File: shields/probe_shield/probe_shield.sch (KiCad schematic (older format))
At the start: 11 parts

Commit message: finished probe shield schematics
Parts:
- added J5: GPIO shield connector 40pin, symbol Connector_Generic:Conn_02x20_Odd_Even
- added J6: probe shield connector 20pin, symbol Connector_Generic:Conn_02x10_Odd_Even
- gave numbers to parts that had none: 11
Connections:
- net +5V: now also J5.2 (Pin_2), J5.4 (Pin_4)
- net GND: now also J5.14 (Pin_14), J5.20 (Pin_20), J5.25 (Pin_25), J5.30 (Pin_30), J5.34 (Pin_34), J5.39 (Pin_39), J5.6 (Pin_6), J5.9 (Pin_9)
- net RST_0: now also J6.9 (Pin_9); no longer J4.10 (~RESET~)
- net RST_1: now also J6.10 (Pin_10)
- net RST_2: now also J6.19 (Pin_19)
- net TCK|SWDCLK_0: now also J6.3 (Pin_3); no longer J4.04 (SWDCLK/TCK)
- net TCK|SWDCLK_1: now also J6.4 (Pin_4)
- net TCK|SWDCLK_2: now also J6.13 (Pin_13)
- net TDI|NC_0: now also J6.7 (Pin_7); no longer J4.08 (NC/TDI)
- net TDI|NC_1: now also J6.8 (Pin_8)
- net TDI|NC_2: now also J6.17 (Pin_17)
- net TDO|SWO_0: now also J6.5 (Pin_5); no longer J4.06 (SWO/TDO)
- net TDO|SWO_1: now also J6.6 (Pin_6)
- net TDO|SWO_2: now also J6.15 (Pin_15)
- net TMS|SWDIO_0: now also J6.1 (Pin_1); no longer J4.02 (SWDIO/TMS)
- net TMS|SWDIO_1: now also J6.2 (Pin_2)
- net TMS|SWDIO_2: now also J6.11 (Pin_11)
- new net RST_3: J4.10 (~RESET~), J6.20 (Pin_20)
- new net TCK|SWDCLK_3: J4.04 (SWDCLK/TCK), J6.14 (Pin_14)
- new net TDI|NC_3: J4.08 (NC/TDI), J6.18 (Pin_18)
- new net TDO|SWO_3: J4.06 (SWO/TDO), J6.16 (Pin_16)
- new net TMS|SWDIO_3: J4.02 (SWDIO/TMS), J6.12 (Pin_12)
- no-connect marks 1 -> 31
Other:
- note added: "GPIO Shield Connector\n(Connects to rpi 40pin header)"
- note added: "Probe Shield Connector"

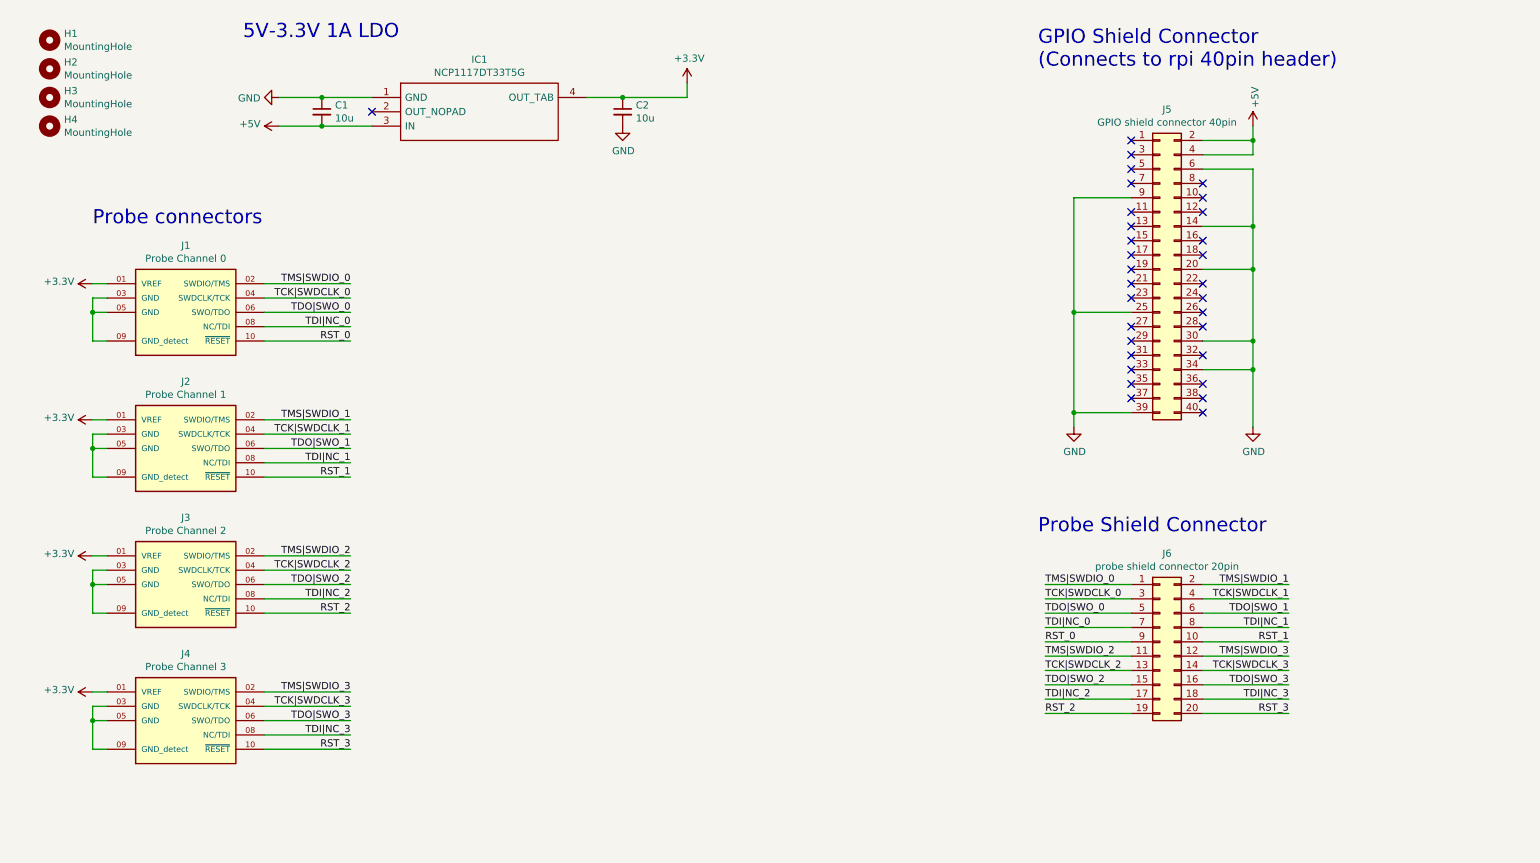
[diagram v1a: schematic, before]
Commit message: added power LED + corrections on probe shield schematics
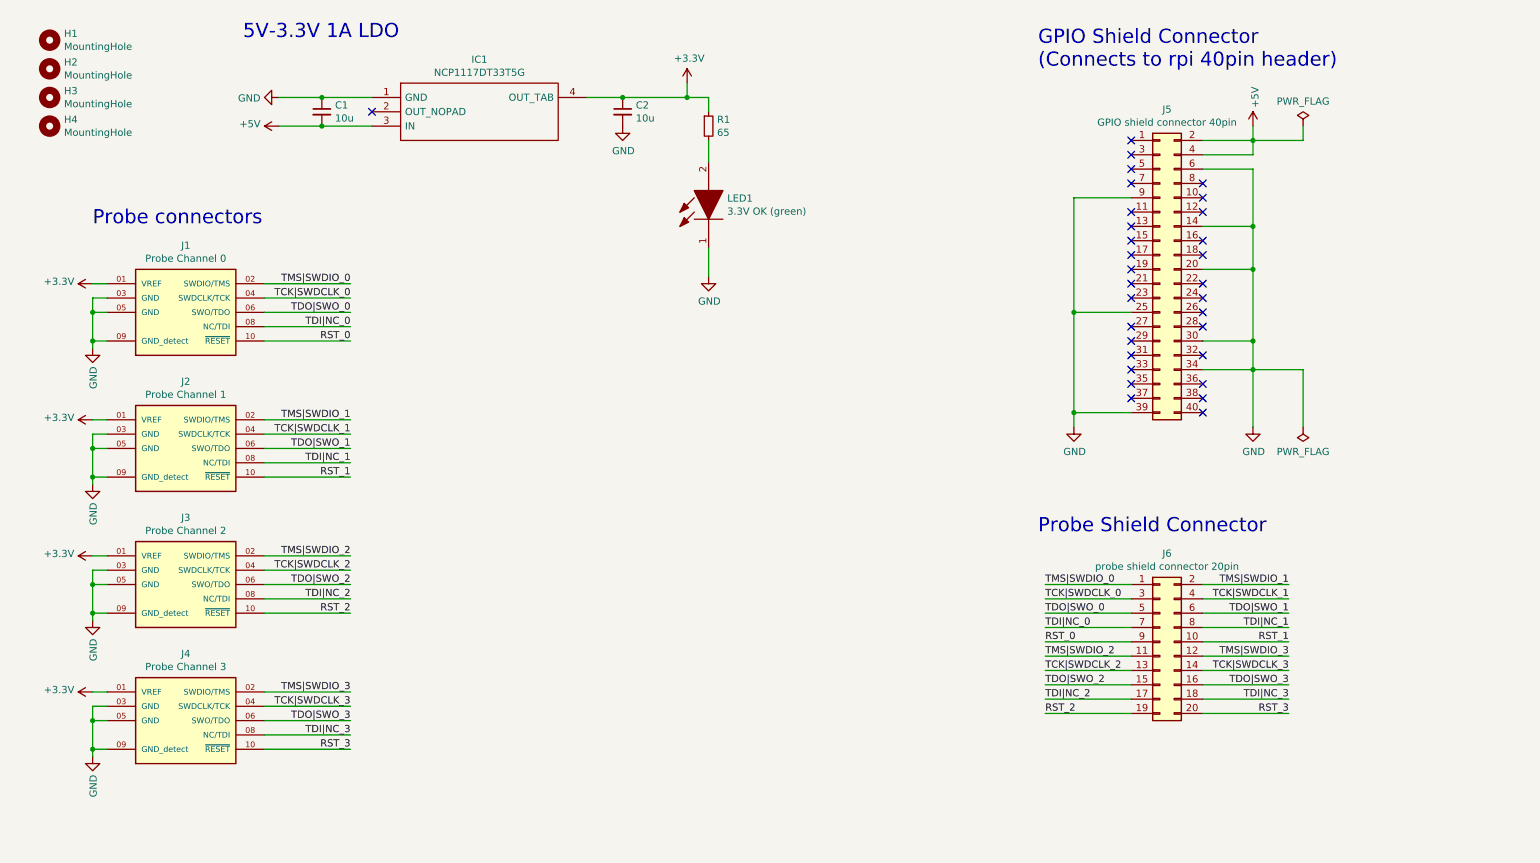
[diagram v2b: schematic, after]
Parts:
- added LED1: 3.3V OK (green), LEDC1608X80N, symbol hive:150060VS75000
- added R1: 65, symbol Device:R_Small
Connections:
- net +3V3: now also R1.1
- net GND: now also J1.03 (GND), J1.05 (GND), J1.09 (GND_detect), J2.03 (GND), J2.05 (GND), J2.09 (GND_detect), J3.03 (GND), J3.05 (GND), J3.09 (GND_detect), J4.03 (GND), J4.05 (GND), J4.09 (GND_detect), LED1.1
- new net: LED1.2, R1.2
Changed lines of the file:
@@
 Text Label 9550 5500 2    50   ~ 0
 RST_3
+$Comp
+L Device:R_Small R1
+U 1 1 61575DED
+P 5500 1400
+F 0 "R1" H 5559 1446 50  0000 L CNN
+F 1 "65" H 5559 1355 50  0000 L CNN
+F 2 "" H 5500 1400 50  0001 C CNN
+F 3 "~" H 5500 1400 50  0001 C CNN
+	1    5500 1400
+	1    0    0    -1
+$EndComp
+Wire Wire Line
+	5500 1300 5500 1200
+Wire Wire Line
+	5500 1200 5350 1200
+Connection ~ 5350 1200
+$Comp
+L hive:150060VS75000 LED1
+U 1 1 6158BF42
+P 5500 2250
+F 0 "LED1" V 5846 2120 50  0000 R CNN
+F 1 "3.3V OK (green)" V 5755 2120 50  0000 R CNN
+F 2 "LEDC1608X80N" H 6000 2400 50  0001 L BNN
+F 3 "https://componentsearchengine.com/Datasheets/2/150060VS75000.pdf" H 6000 2300 50  0001 L BNN
+F 4 "2.4 V Green LED 1608 (0603) SMD, Wurth Elektronik WL-SMCW 150060VS75000" H 6000 2200 50  0001 L BNN "Description"
+F 5 "0.8" H 6000 2100 50  0001 L BNN "Height"
+F 6 "710-150060VS75000" H 6000 2000 50  0001 L BNN "Mouser Part Number"
+F 7 "https://www.mouser.co.uk/ProductDetail/Wurth-Elektronik/150060VS75000?qs=LlUlMxKIyB1Q1Bi5mQ%2FKLw%3D%3D" H 6000 1900 50  0001 L BNN "Mouser Price/Stock"
+F 8 "Wurth Elektronik" H 6000 1800 50  0001 L BNN "Manufacturer_Name"
+F 9 "150060VS75000" H 6000 1700 50  0001 L BNN "Manufacturer_Part_Number"
+	1    5500 2250
+	0    -1   -1   0
+$EndComp
+$Comp
+L power:GND #PWR012
+U 1 1 6158E94E
+P 5500 2450
+F 0 "#PWR012" H 5500 2200 50  0001 C CNN
+F 1 "GND" H 5505 2277 50  0000 C CNN
+F 2 "" H 5500 2450 50  0001 C CNN
+F 3 "" H 5500 2450 50  0001 C CNN
+	1    5500 2450
+	1    0    0    -1
+$EndComp
+Wire Wire Line
+	5500 2450 5500 2250
+Wire Wire Line
+	5500 1650 5500 1500
+Wire Wire Line
+	9300 1500 9650 1500
+Wire Wire Line
+	9650 1500 9650 1400
+$Comp
+L power:PWR_FLAG #FLG0101
+U 1 1 6159857E
+P 9650 1400
+F 0 "#FLG0101" H 9650 1475 50  0001 C CNN
+F 1 "PWR_FLAG" H 9650 1573 50  0000 C CNN
+F 2 "" H 9650 1400 50  0001 C CNN
+F 3 "~" H 9650 1400 50  0001 C CNN
+	1    9650 1400
+	1    0    0    -1
+$EndComp
+$Comp
+L power:PWR_FLAG #FLG0102
+U 1 1 6159C7A5
+P 9650 3500
+F 0 "#FLG0102" H 9650 3575 50  0001 C CNN
+F 1 "PWR_FLAG" H 9650 3673 50  0000 C CNN
+F 2 "" H 9650 3500 50  0001 C CNN
+F 3 "~" H 9650 3500 50  0001 C CNN
+	1    9650 3500
+	-1   0    0    1
+$EndComp
+Wire Wire Line
+	9650 3500 9650 3100
+Wire Wire Line
+	9650 3100 9300 3100
+$Comp
+L power:GND #PWR0101
+U 1 1 615A158D
+P 1200 2950
+F 0 "#PWR0101" H 1200 2700 50  0001 C CNN
+F 1 "GND" V 1205 2822 50  0000 R CNN
+F 2 "" H 1200 2950 50  0001 C CNN
+F 3 "" H 1200 2950 50  0001 C CNN
+	1    1200 2950
+	1    0    0    -1
+$EndComp
+$Comp
+L power:GND #PWR0102
+U 1 1 615A28FC
+P 1200 3900
+F 0 "#PWR0102" H 1200 3650 50  0001 C CNN
+F 1 "GND" V 1205 3772 50  0000 R CNN
+F 2 "" H 1200 3900 50  0001 C CNN
+F 3 "" H 1200 3900 50  0001 C CNN
+	1    1200 3900
+	1    0    0    -1
+$EndComp
+$Comp
+L power:GND #PWR0103
+U 1 1 615A323E
+P 1200 4850
+F 0 "#PWR0103" H 1200 4600 50  0001 C CNN
+F 1 "GND" V 1205 4722 50  0000 R CNN
+F 2 "" H 1200 4850 50  0001 C CNN
+F 3 "" H 1200 4850 50  0001 C CNN
+	1    1200 4850
+	1    0    0    -1
+$EndComp
+$Comp
+L power:GND #PWR0104
+U 1 1 615A3C39
+P 1200 5800
+F 0 "#PWR0104" H 1200 5550 50  0001 C CNN
+F 1 "GND" V 1205 5672 50  0000 R CNN
+F 2 "" H 1200 5800 50  0001 C CNN
+F 3 "" H 1200 5800 50  0001 C CNN
+	1    1200 5800
+	1    0    0    -1
+$EndComp
+Wire Wire Line
+	1200 5800 1200 5750
+Connection ~ 1200 5750
+Wire Wire Line
+	1200 4850 1200 4800
+Connection ~ 1200 4800
+Wire Wire Line
+	1200 3900 1200 3850
+Connection ~ 1200 3850
+Wire Wire Line
+	1200 2950 1200 2900
+Connection ~ 1200 2900
 $EndSCHEMATC

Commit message: schematic updates, start of probe shield layout
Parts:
- removed H2, H3, H4: MountingHole, symbol Mechanical:MountingHole
- added H2, H3, H4, H5, H6: MountingHole, MountingHole:MountingHole_2.7mm_M2.5_DIN965_Pad, symbol Mechanical:MountingHole_Pad
- C1, C2: footprint (none) -> Capacitor_SMD:C_0805_2012Metric_Pad1.15x1.40mm_HandSolder
- H1: footprint (none) -> MountingHole:MountingHole_2.7mm_M2.5_DIN965_Pad; symbol Mechanical:MountingHole -> Mechanical:MountingHole_Pad
- IC1: footprint TO229P990X238-4N -> hive:TO229P990X238-4N
- J1, J2, J3, J4: footprint SAMTEC_FTSH-105-01-F-DV-007 -> hive:SAMTEC_FTSH-105-01-F-DV-007
- J5: footprint (none) -> Connector_PinHeader_2.54mm:PinHeader_2x20_P2.54mm_Vertical
- J6: value probe shield connector 20pin -> probe shield connector 20 or 26pin; footprint (none) -> Connector_PinHeader_2.54mm:PinHeader_2x13_P2.54mm_Vertical; symbol Connector_Generic:Conn_02x10_Odd_Even -> Connector_Generic:Conn_02x13_Odd_Even
- R1: footprint (none) -> Resistor_SMD:R_0805_2012Metric_Pad1.15x1.40mm_HandSolder
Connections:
- net GND: now also H1.1, J6.21 (Pin_21), J6.22 (Pin_22), J6.23 (Pin_23), J6.24 (Pin_24), J6.25 (Pin_25), J6.26 (Pin_26), H2.1, H3.1, H4.1, H5.1, H6.1
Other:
- note added: "Last 6 Pins are not required!\nYou may also use a 2x10pin connector \ninstead of a 2x13pin with 2.54mm pitch"
- moved on the sheet: J1, J2, J3, J4

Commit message: implemented changes according to feedback, finished target shield schematics
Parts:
- J6: value probe shield connector 20 or 26pin -> probe shield connector 26pin
- R1: value 65 -> 195
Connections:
- net GND: now also J6.1 (Pin_1), J6.13 (Pin_13), J6.14 (Pin_14), J6.2 (Pin_2); no longer J6.21 (Pin_21), J6.22 (Pin_22), J6.23 (Pin_23), J6.24 (Pin_24)
- net RST_0: now also J6.11 (Pin_11); no longer J6.9 (Pin_9)
- net RST_1: now also J6.12 (Pin_12); no longer J6.10 (Pin_10)
- net RST_2: now also J6.23 (Pin_23); no longer J6.19 (Pin_19)
- net RST_3: now also J6.24 (Pin_24); no longer J6.20 (Pin_20)
- net TCK|SWDCLK_0: now also J6.5 (Pin_5); no longer J6.3 (Pin_3)
- net TCK|SWDCLK_1: now also J6.6 (Pin_6); no longer J6.4 (Pin_4)
- net TCK|SWDCLK_2: now also J6.17 (Pin_17); no longer J6.13 (Pin_13)
- net TCK|SWDCLK_3: now also J6.18 (Pin_18); no longer J6.14 (Pin_14)
- net TDI|NC_0: now also J6.9 (Pin_9); no longer J6.7 (Pin_7)
- net TDI|NC_1: now also J6.10 (Pin_10); no longer J6.8 (Pin_8)
- net TDI|NC_2: now also J6.21 (Pin_21); no longer J6.17 (Pin_17)
- net TDI|NC_3: now also J6.22 (Pin_22); no longer J6.18 (Pin_18)
- net TDO|SWO_0: now also J6.7 (Pin_7); no longer J6.5 (Pin_5)
- net TDO|SWO_1: now also J6.8 (Pin_8); no longer J6.6 (Pin_6)
- net TDO|SWO_2: now also J6.19 (Pin_19); no longer J6.15 (Pin_15)
- net TDO|SWO_3: now also J6.20 (Pin_20); no longer J6.16 (Pin_16)
- net TMS|SWDIO_0: now also J6.3 (Pin_3); no longer J6.1 (Pin_1)
- net TMS|SWDIO_1: now also J6.4 (Pin_4); no longer J6.2 (Pin_2)
- net TMS|SWDIO_2: now also J6.15 (Pin_15); no longer J6.11 (Pin_11)
- net TMS|SWDIO_3: now also J6.16 (Pin_16); no longer J6.12 (Pin_12)
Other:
- note removed: "Last 6 Pins are not required!\nYou may also use a 2x10pin connector \ninstead of a 2x13pin with 2.54mm pitch"
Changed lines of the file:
@@
 P 8650 5200
 F 0 "J6" H 8700 6050 50  0000 C CNN
-F 1 "probe shield connector 20 or 26pin" H 8700 5950 50  0000 C CNN
+F 1 "probe shield connector 26pin" H 8700 5950 50  0000 C CNN
 F 2 "Connector_PinHeader_2.54mm:PinHeader_2x13_P2.54mm_Vertical" H 8650 5200 50  0001 C CNN
 F 3 "~" H 8650 5200 50  0001 C CNN
@@
 NoConn ~ 8950 3400
 Wire Wire Line
-	8450 4600 7850 4600
-Wire Wire Line
 	8450 4700 7850 4700
 Wire Wire Line
@@
 Wire Wire Line
 	8450 5000 7850 5000
-Text Label 7850 4600 0    50   ~ 0
+Wire Wire Line
+	8450 5100 7850 5100
+Text Label 7850 4700 0    50   ~ 0
 TMS|SWDIO_0
-Text Label 7850 4700 0    50   ~ 0
+Text Label 7850 4800 0    50   ~ 0
 TCK|SWDCLK_0
-Text Label 7850 4800 0    50   ~ 0
+Text Label 7850 4900 0    50   ~ 0
 TDO|SWO_0
-Text Label 7850 4900 0    50   ~ 0
+Text Label 7850 5000 0    50   ~ 0
 TDI|NC_0
-Text Label 7850 5000 0    50   ~ 0
+Text Label 7850 5100 0    50   ~ 0
 RST_0
 Wire Wire Line
-	8450 5100 7850 5100
-Wire Wire Line
-	8450 5200 7850 5200
-Wire Wire Line
 	8450 5300 7850 5300
 Wire Wire Line
@@
 Wire Wire Line
 	8450 5500 7850 5500
-Text Label 7850 5100 0    50   ~ 0
+Wire Wire Line
+	8450 5600 7850 5600
+Wire Wire Line
+	8450 5700 7850 5700
+Text Label 7850 5300 0    50   ~ 0
 TMS|SWDIO_2
-Text Label 7850 5200 0    50   ~ 0
+Text Label 7850 5400 0    50   ~ 0
 TCK|SWDCLK_2
-Text Label 7850 5300 0    50   ~ 0
+Text Label 7850 5500 0    50   ~ 0
 TDO|SWO_2
-Text Label 7850 5400 0    50   ~ 0
+Text Label 7850 5600 0    50   ~ 0
 TDI|NC_2
-Text Label 7850 5500 0    50   ~ 0
+Text Label 7850 5700 0    50   ~ 0
 RST_2
 Wire Wire Line
-	8950 4600 9550 4600
-Wire Wire Line
 	8950 4700 9550 4700
 Wire Wire Line
@@
 Wire Wire Line
 	8950 5000 9550 5000
-Text Label 9550 4600 2    50   ~ 0
+Wire Wire Line
+	8950 5100 9550 5100
+Text Label 9550 4700 2    50   ~ 0
 TMS|SWDIO_1
-Text Label 9550 4700 2    50   ~ 0
+Text Label 9550 4800 2    50   ~ 0
 TCK|SWDCLK_1
-Text Label 9550 4800 2    50   ~ 0
+Text Label 9550 4900 2    50   ~ 0
 TDO|SWO_1
-Text Label 9550 4900 2    50   ~ 0
+Text Label 9550 5000 2    50   ~ 0
 TDI|NC_1
-Text Label 9550 5000 2    50   ~ 0
+Text Label 9550 5100 2    50   ~ 0
 RST_1
 Wire Wire Line
-	8950 5100 9550 5100
-Wire Wire Line
-	8950 5200 9550 5200
-Wire Wire Line
 	8950 5300 9550 5300
 Wire Wire Line
@@
 Wire Wire Line
 	8950 5500 9550 5500
-Text Label 9550 5100 2    50   ~ 0
+Wire Wire Line
+	8950 5600 9550 5600
+Wire Wire Line
+	8950 5700 9550 5700
+Text Label 9550 5300 2    50   ~ 0
 TMS|SWDIO_3
-Text Label 9550 5200 2    50   ~ 0
+Text Label 9550 5400 2    50   ~ 0
 TCK|SWDCLK_3
-Text Label 9550 5300 2    50   ~ 0
+Text Label 9550 5500 2    50   ~ 0
 TDO|SWO_3
-Text Label 9550 5400 2    50   ~ 0
+Text Label 9550 5600 2    50   ~ 0
 TDI|NC_3
-Text Label 9550 5500 2    50   ~ 0
+Text Label 9550 5700 2    50   ~ 0
 RST_3
 $Comp
@@
 P 5500 1400
 F 0 "R1" H 5559 1446 50  0000 L CNN
-F 1 "65" H 5559 1355 50  0000 L CNN
+F 1 "195" H 5559 1355 50  0000 L CNN
 F 2 "Resistor_SMD:R_0805_2012Metric_Pad1.15x1.40mm_HandSolder" H 5500 1400 50  0001 C CNN
 F 3 "~" H 5500 1400 50  0001 C CNN
@@
 	1200 3300 1200 3250
 Connection ~ 1200 3250
-Wire Wire Line
-	8450 5600 8300 5600
-Wire Wire Line
-	8300 5600 8300 5700
-Wire Wire Line
-	8300 5950 8700 5950
-Wire Wire Line
-	9100 5950 9100 5800
-Wire Wire Line
-	9100 5600 8950 5600
-Wire Wire Line
-	8950 5700 9100 5700
-Connection ~ 9100 5700
-Wire Wire Line
-	9100 5700 9100 5600
-Wire Wire Line
-	8950 5800 9100 5800
-Connection ~ 9100 5800
-Wire Wire Line
-	9100 5800 9100 5700
-Wire Wire Line
-	8450 5700 8300 5700
-Connection ~ 8300 5700
-Wire Wire Line
-	8300 5700 8300 5800
-Wire Wire Line
-	8450 5800 8300 5800
-Connection ~ 8300 5800
-Wire Wire Line
-	8300 5800 8300 5950
-$Comp
-L power:GND #PWR013
-U 1 1 6155CE20
-P 8700 6050
-F 0 "#PWR013" H 8700 5800 50  0001 C CNN
-F 1 "GND" H 8705 5877 50  0000 C CNN
-F 2 "" H 8700 6050 50  0001 C CNN
-F 3 "" H 8700 6050 50  0001 C CNN
-	1    8700 6050
-	1    0    0    -1
-$EndComp
-Wire Wire Line
-	8700 6050 8700 5950
-Connection ~ 8700 5950
-Wire Wire Line
-	8700 5950 9100 5950
-Wire Notes Line
-	8150 6000 8150 5550
-Wire Notes Line
-	8150 5550 9250 5550
-Wire Notes Line
-	9250 5550 9250 6000
-Wire Notes Line
-	8150 6000 9250 6000
-Text Notes 9350 5850 0    50   ~ 0
-Last 6 Pins are not required!\nYou may also use a 2x10pin connector \ninstead of a 2x13pin with 2.54mm pitch
 $Comp
 L Mechanical:MountingHole_Pad H2
@@
 	0    -1   -1   0
 $EndComp
+$Comp
+L power:GND #PWR?
+U 1 1 6158CD45
+P 7750 4600
+F 0 "#PWR?" H 7750 4350 50  0001 C CNN
+F 1 "GND" V 7750 4400 50  0000 C CNN
+F 2 "" H 7750 4600 50  0001 C CNN
+F 3 "" H 7750 4600 50  0001 C CNN
+	1    7750 4600
+	0    1    1    0
+$EndComp
+Wire Wire Line
+	8450 4600 7750 4600
+$Comp
+L power:GND #PWR?
+U 1 1 61593F46
+P 7750 5200
+F 0 "#PWR?" H 7750 4950 50  0001 C CNN
+F 1 "GND" V 7750 5000 50  0000 C CNN
+F 2 "" H 7750 5200 50  0001 C CNN
+F 3 "" H 7750 5200 50  0001 C CNN
+	1    7750 5200
+	0    1    1    0
+$EndComp
+Wire Wire Line
+	8450 5200 7750 5200
+$Comp
+L power:GND #PWR?
+U 1 1 61598641
+P 7750 5800
+F 0 "#PWR?" H 7750 5550 50  0001 C CNN
+F 1 "GND" V 7750 5600 50  0000 C CNN
+F 2 "" H 7750 5800 50  0001 C CNN
+F 3 "" H 7750 5800 50  0001 C CNN
+	1    7750 5800
+	0    1    1    0
+$EndComp
+Wire Wire Line
+	8450 5800 7750 5800
+$Comp
+L power:GND #PWR?
+U 1 1 6159D4B7
+P 9650 5800
+F 0 "#PWR?" H 9650 5550 50  0001 C CNN
+F 1 "GND" V 9650 5600 50  0000 C CNN
+F 2 "" H 9650 5800 50  0001 C CNN
+F 3 "" H 9650 5800 50  0001 C CNN
+	1    9650 5800
+	0    -1   -1   0
+$EndComp
+Wire Wire Line
+	8950 5800 9650 5800
+$Comp
+L power:GND #PWR?
+U 1 1 615A1DEC
+P 9650 5200
+F 0 "#PWR?" H 9650 4950 50  0001 C CNN
+F 1 "GND" V 9650 5000 50  0000 C CNN
+F 2 "" H 9650 5200 50  0001 C CNN
+F 3 "" H 9650 5200 50  0001 C CNN
+	1    9650 5200
+	0    -1   -1   0
+$EndComp
+Wire Wire Line
+	8950 5200 9650 5200
+$Comp
+L power:GND #PWR?
+U 1 1 615A63BC
+P 9650 4600
+F 0 "#PWR?" H 9650 4350 50  0001 C CNN
+F 1 "GND" V 9650 4400 50  0000 C CNN
+F 2 "" H 9650 4600 50  0001 C CNN
+F 3 "" H 9650 4600 50  0001 C CNN
+	1    9650 4600
+	0    -1   -1   0
+$EndComp
+Wire Wire Line
+	8950 4600 9650 4600
 $EndSCHEMATC
